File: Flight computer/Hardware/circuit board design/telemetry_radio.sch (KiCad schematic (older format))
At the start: 31 parts, among them U2 AS179-92LF, U3 Si4463, X1 TM-32.000-AF3-33-S-Oscillator

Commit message: added in the RF front end, exactly as stated in AN904
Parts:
- removed ANT2: ICSSPicoTracker_Yageo434, pico_tracker:Yageo434, symbol flight-computer:ICSSPicoTracker_Yageo434
- removed C11, C12, C13: 150pF, Capacitor_SMD:C_0402_1005Metric, symbol Device:C_Small
- removed C14: 12pF, Capacitor_SMD:C_0402_1005Metric, symbol Device:C_Small
- removed C15: 33pF, Capacitor_SMD:C_0402_1005Metric, symbol Device:C_Small
- removed C16: 15pF, Capacitor_SMD:C_0402_1005Metric, symbol Device:C_Small
- removed C17, C27: 4.7pF, Capacitor_SMD:C_0402_1005Metric, symbol Device:C_Small
- removed C18: 9.1pF, Capacitor_SMD:C_0402_1005Metric, symbol Device:C_Small
- removed C24, C25: 1nF, Capacitor_SMD:C_0402_1005Metric, symbol Device:C_Small
- removed C26, C8: NF, Capacitor_SMD:C_0402_1005Metric, symbol Device:C_Small
- removed L2: 0R, Inductor_SMD:L_0402_1005Metric, symbol Device:L
- removed L3: 18nH, Inductor_SMD:L_0402_1005Metric, symbol Device:L
- removed L4: 30nH, Inductor_SMD:L_0402_1005Metric, symbol Device:L
- removed L5: 22nH, Inductor_SMD:L_0402_1005Metric, symbol Device:L
- removed L6, L7: 62nH, Inductor_SMD:L_0402_1005Metric, symbol Device:L
- removed U2: AS179-92LF, Package_TO_SOT_SMD:SOT-363_SC-70-6, symbol RF_Switch:AS179-92LF
- added AE1: Antenna, symbol Device:Antenna
- added C9: 270pF, Capacitor_SMD:C_0402_1005Metric, symbol Device:C_Small
- added J7: Conn_Coaxial, symbol Connector:Conn_Coaxial
- added R4: 0R, symbol Device:R
- added R7: NF, symbol Device:R
- C10: value 2.2uF -> CA
- C19: value 100nf -> 270pf
- gave numbers to parts that had none: 1
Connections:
- net labels removed: RF_GPIO0, RF_GPIO1
- wire segments 112 -> 63
- no-connect marks 4 -> 3
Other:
- note removed: "434 Mhz Antenna Match/Filter"
- note removed: "RF switch"
- note removed: "Rx Balun"
- note removed: "TX Match"
- note removed: "Tx Low Pass Filter"
- moved on the sheet: U2

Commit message: fixed erc problems with Johanson integrated Frontend.
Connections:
- net labels added: RF_GPIO0, RF_GPIO1
- wire segments 63 -> 65
- no-connect marks 3 -> 5
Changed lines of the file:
@@
 Wire Wire Line
 	10050 3650 10050 3900
+Text HLabel 4450 4950 2    50   Input ~ 0
+RF_GPIO0
+Wire Wire Line
+	4450 4950 4200 4950
+Text HLabel 4450 5050 2    50   Input ~ 0
+RF_GPIO1
+Wire Wire Line
+	4450 5050 4200 5050
+NoConn ~ 4200 5250
+NoConn ~ 4200 5150
 $EndSCHEMATC

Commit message: added in some comments
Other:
- note added: "Antenna is wire at 1/4 wavelength. ~17cm"
- note added: "Arranged according to Silabs AN904"
- note added: "Not sure if I should put in the Pi circuit"
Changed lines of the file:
@@
 Sheet 4 7
 Title "Silabs radio chip for telemetry to ground"
-Date "2019-08-31"
-Rev ""
+Date "2019-09-09"
+Rev "1.0"
 Comp "Imperial College Space Society"
-Comment1 "AN629 Figure 16 ideal according to Richard: CLE Switch TX/RX type matching network"
-Comment2 "AN648 for matching network values"
+Comment1 "Arranged according to Silabs AN904."
+Comment2 ""
 Comment3 ""
 Comment4 ""
@@
 NoConn ~ 4200 5250
 NoConn ~ 4200 5150
+Text Notes 8750 2500 0    50   ~ 0
+Not sure if I should put in the Pi circuit
+Text Notes 8800 2700 0    50   ~ 0
+Antenna is wire at 1/4 wavelength. ~17cm
+Text Notes 4550 6100 0    50   ~ 0
+Arranged according to Silabs AN904
 $EndSCHEMATC

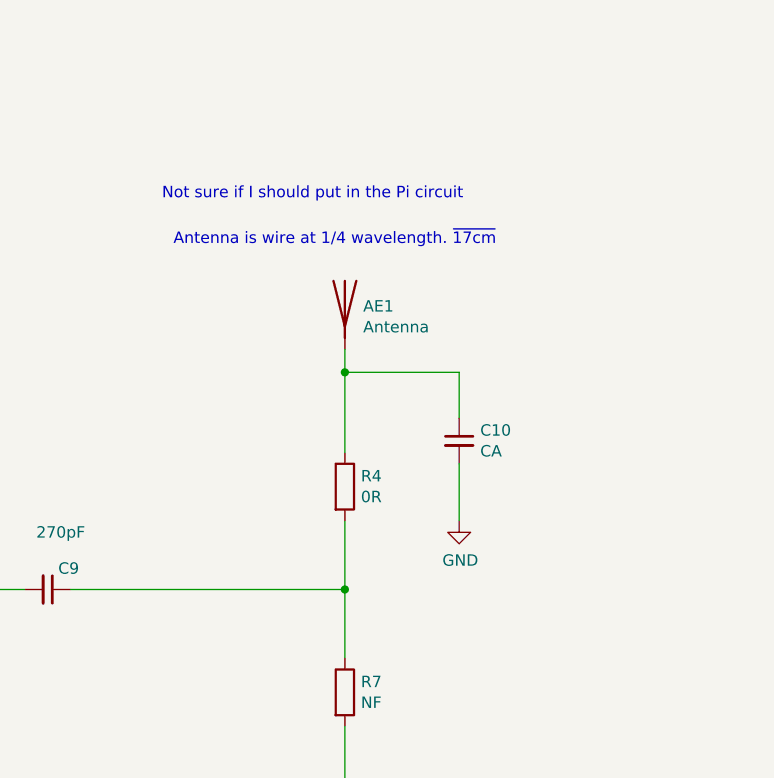
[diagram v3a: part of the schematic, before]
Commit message: completed the pi circuit for Telemetry antenna
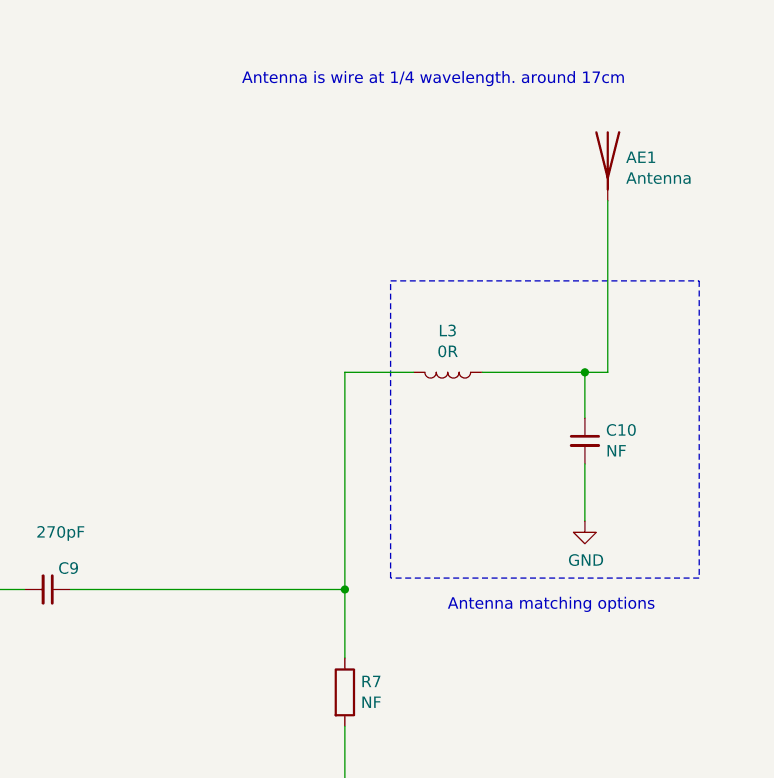
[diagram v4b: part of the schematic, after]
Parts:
- removed R4: 0R, symbol Device:R
- added L3: 0R, Inductor_SMD:L_0402_1005Metric, symbol Device:L
- C10: value CA -> NF
- R7: footprint (none) -> Resistor_SMD:R_0402_1005Metric
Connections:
- wire segments 65 -> 66
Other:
- note added: "Antenna is wire at 1/4 wavelength. around 17cm"
- note added: "Antenna matching options\n"
- note removed: "Antenna is wire at 1/4 wavelength. ~17cm"
- note removed: "Not sure if I should put in the Pi circuit"
- moved on the sheet: AE1
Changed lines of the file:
@@
 L Device:Antenna AE1
 U 1 1 5D79EB91
-P 9550 2950
-F 0 "AE1" H 9630 2939 50  0000 L CNN
-F 1 "Antenna" H 9630 2848 50  0000 L CNN
-F 2 "" H 9550 2950 50  0001 C CNN
-F 3 "~" H 9550 2950 50  0001 C CNN
-	1    9550 2950
+P 10700 2300
+F 0 "AE1" H 10780 2289 50  0000 L CNN
+F 1 "Antenna" H 10780 2198 50  0000 L CNN
+F 2 "" H 10700 2300 50  0001 C CNN
+F 3 "~" H 10700 2300 50  0001 C CNN
+	1    10700 2300
 	1    0    0    -1
 $EndComp
 Wire Wire Line
-	9550 3150 9550 3250
-Wire Wire Line
-	9550 3250 10050 3250
-Wire Wire Line
-	10050 3250 10050 3450
-Connection ~ 9550 3250
-Wire Wire Line
-	9550 3250 9550 3600
-$Comp
-L power:GND #PWR017
-U 1 1 5D7A234E
-P 10050 3900
-F 0 "#PWR017" H 10050 3650 50  0001 C CNN
-F 1 "GND" H 10055 3727 50  0000 C CNN
-F 2 "" H 10050 3900 50  0001 C CNN
-F 3 "" H 10050 3900 50  0001 C CNN
-	1    10050 3900
-	1    0    0    -1
-$EndComp
+	10700 2500 10700 3250
 $Comp
 L Connector:Conn_Coaxial J7
@@
 	3700 2550 3700 2800
 $Comp
-L Device:R R4
-U 1 1 5D7AAB64
-P 9550 3750
-F 0 "R4" H 9620 3796 50  0000 L CNN
-F 1 "0R" H 9620 3705 50  0000 L CNN
-F 2 "" V 9480 3750 50  0001 C CNN
-F 3 "~" H 9550 3750 50  0001 C CNN
-	1    9550 3750
-	1    0    0    -1
-$EndComp
-Wire Wire Line
-	9550 3900 9550 4200
-$Comp
 L Device:R R7
 U 1 1 5D7AB0E5
@@
 F 0 "R7" H 9620 4696 50  0000 L CNN
 F 1 "NF" H 9620 4605 50  0000 L CNN
-F 2 "" V 9480 4650 50  0001 C CNN
+F 2 "Resistor_SMD:R_0402_1005Metric" V 9480 4650 50  0001 C CNN
 F 3 "~" H 9550 4650 50  0001 C CNN
 	1    9550 4650
@@
 Wire Wire Line
 	9550 4800 9550 5050
-$Comp
-L Device:C_Small C10
-U 1 1 5D7AB505
-P 10050 3550
-F 0 "C10" H 9958 3596 50  0000 R CNN
-F 1 "CA" H 9958 3505 50  0000 R CNN
-F 2 "Capacitor_SMD:C_0603_1608Metric" H 10050 3550 50  0001 C CNN
-F 3 "~" H 10050 3550 50  0001 C CNN
-	1    10050 3550
-	-1   0    0    -1
-$EndComp
-Wire Wire Line
-	10050 3650 10050 3900
 Text HLabel 4450 4950 2    50   Input ~ 0
 RF_GPIO0
@@
 NoConn ~ 4200 5250
 NoConn ~ 4200 5150
-Text Notes 8750 2500 0    50   ~ 0
-Not sure if I should put in the Pi circuit
-Text Notes 8800 2700 0    50   ~ 0
-Antenna is wire at 1/4 wavelength. ~17cm
+Text Notes 9100 2000 0    50   ~ 0
+Antenna is wire at 1/4 wavelength. around 17cm
 Text Notes 4550 6100 0    50   ~ 0
 Arranged according to Silabs AN904
+Wire Wire Line
+	10150 3250 10600 3250
+Wire Wire Line
+	9550 3250 9550 4200
+Wire Wire Line
+	10600 3650 10600 3900
+$Comp
+L Device:C_Small C10
+U 1 1 5D7EC7D6
+P 10600 3550
+F 0 "C10" H 10508 3596 50  0000 R CNN
+F 1 "NF" H 10508 3505 50  0000 R CNN
+F 2 "Capacitor_SMD:C_0603_1608Metric" H 10600 3550 50  0001 C CNN
+F 3 "~" H 10600 3550 50  0001 C CNN
+	1    10600 3550
+	-1   0    0    -1
+$EndComp
+$Comp
+L power:GND #PWR07
+U 1 1 5D7EC7E0
+P 10600 3900
+F 0 "#PWR07" H 10600 3650 50  0001 C CNN
+F 1 "GND" H 10605 3727 50  0000 C CNN
+F 2 "" H 10600 3900 50  0001 C CNN
+F 3 "" H 10600 3900 50  0001 C CNN
+	1    10600 3900
+	1    0    0    -1
+$EndComp
+Wire Wire Line
+	10600 3250 10600 3450
+Connection ~ 10600 3250
+Wire Wire Line
+	10600 3250 10700 3250
+Text Notes 10000 4300 0    50   ~ 0
+Antenna matching options\n
+Wire Wire Line
+	9550 3250 9850 3250
+$Comp
+L Device:L L3
+U 1 1 5D7F0545
+P 10000 3250
+F 0 "L3" V 9819 3250 50  0000 C CNN
+F 1 "0R" V 9910 3250 50  0000 C CNN
+F 2 "Inductor_SMD:L_0402_1005Metric" H 10000 3250 50  0001 C CNN
+F 3 "~" H 10000 3250 50  0001 C CNN
+	1    10000 3250
+	0    1    1    0
+$EndComp
+Wire Notes Line
+	11100 4150 9750 4150
+Wire Notes Line
+	9750 4150 9750 2850
+Wire Notes Line
+	9750 2850 11100 2850
+Wire Notes Line
+	11100 2850 11100 4150
 $EndSCHEMATC

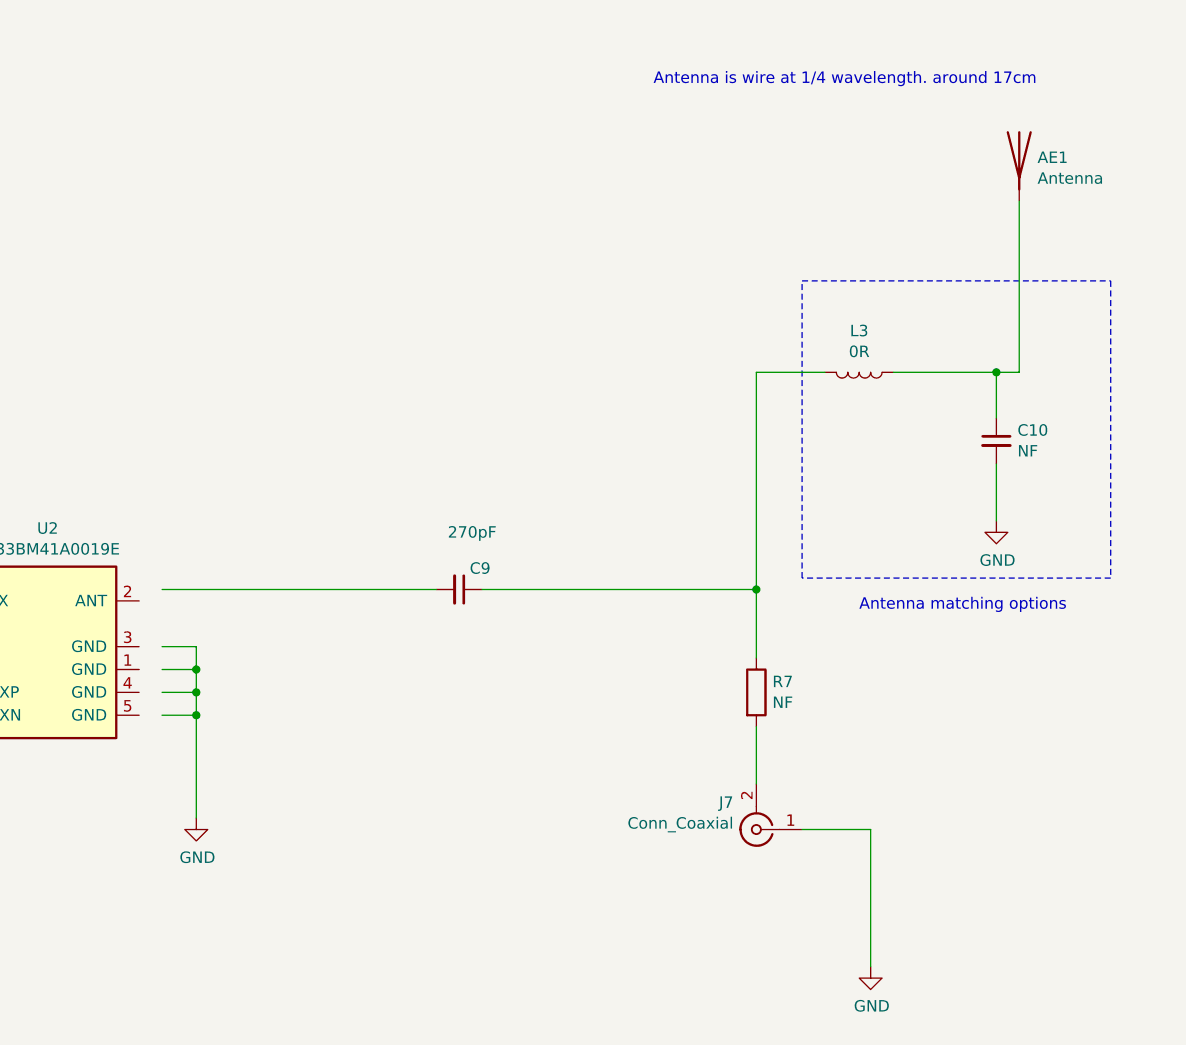
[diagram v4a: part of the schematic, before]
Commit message: changed the pin header to 2.54mm pitch for programmer and added a 3 pin header for antenna 434
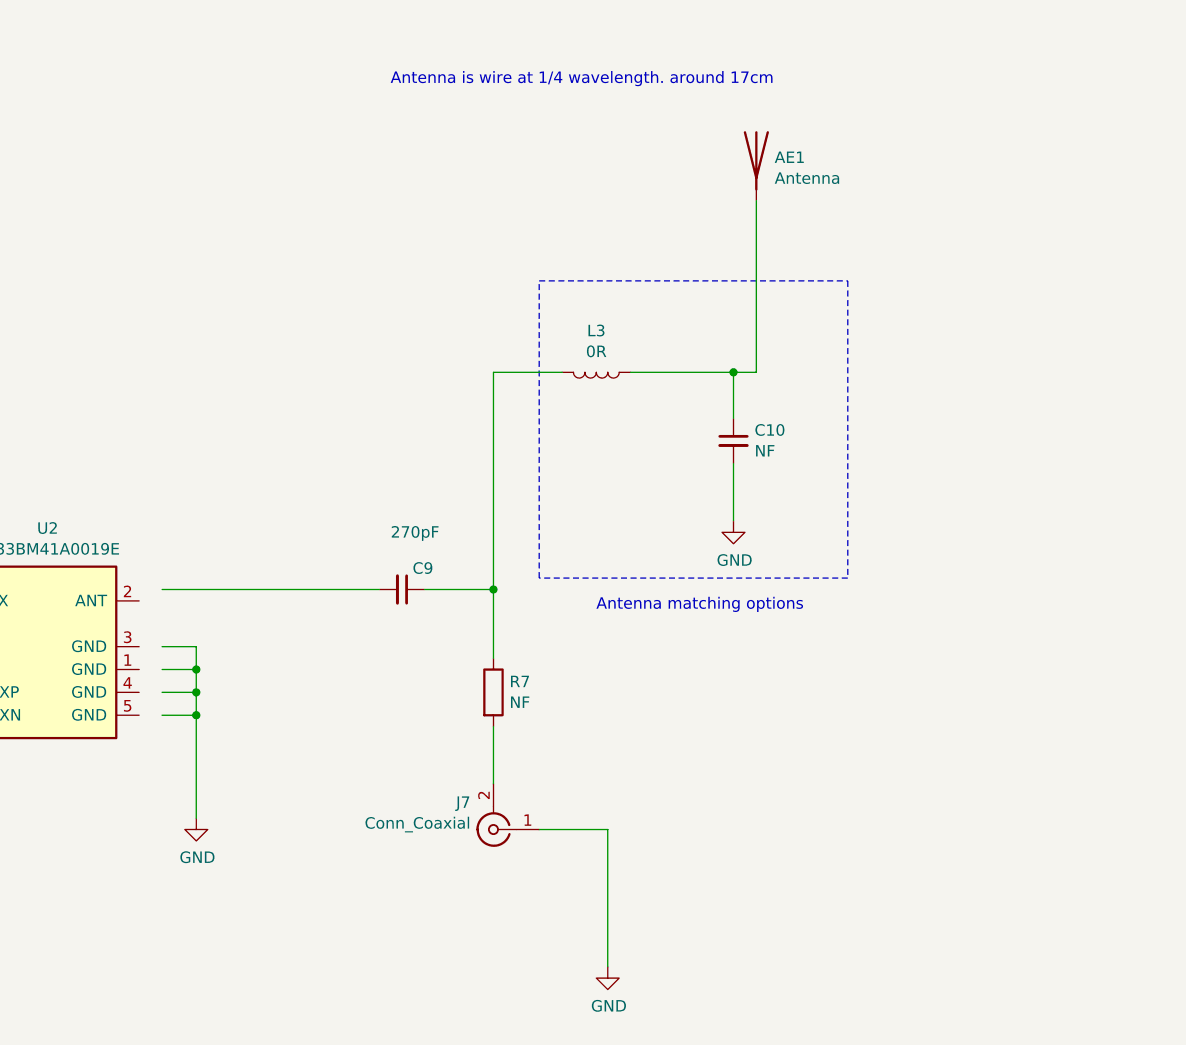
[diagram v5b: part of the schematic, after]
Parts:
- AE1: footprint (none) -> Connector_PinHeader_1.00mm:PinHeader_1x03_P1.00mm_Vertical
- J7: footprint (none) -> Connector_Coaxial:U.FL_Hirose_U.FL-R-SMT-1_Vertical
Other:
- moved on the sheet: AE1, C10, C9, J7, L3, R7
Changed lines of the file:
@@
 $EndComp
 Wire Wire Line
-	6950 4200 8150 4200
+	6950 4200 7900 4200
 $Comp
 L Device:C_Small C9
 U 1 1 5D796ABE
-P 8250 4200
-F 0 "C9" V 8342 4246 50  0000 L CNN
-F 1 "270pF" V 8500 4150 50  0000 L CNN
-F 2 "Capacitor_SMD:C_0402_1005Metric" H 8250 4200 50  0001 C CNN
-F 3 "~" H 8250 4200 50  0001 C CNN
-	1    8250 4200
+P 8000 4200
+F 0 "C9" V 8092 4246 50  0000 L CNN
+F 1 "270pF" V 8250 4150 50  0000 L CNN
+F 2 "Capacitor_SMD:C_0402_1005Metric" H 8000 4200 50  0001 C CNN
+F 3 "~" H 8000 4200 50  0001 C CNN
+	1    8000 4200
 	0    1    -1   0
-$EndComp
-Wire Wire Line
-	8350 4200 9550 4200
-Wire Wire Line
-	9550 4200 9550 4500
-Connection ~ 9550 4200
-$Comp
-L Device:Antenna AE1
-U 1 1 5D79EB91
-P 10700 2300
-F 0 "AE1" H 10780 2289 50  0000 L CNN
-F 1 "Antenna" H 10780 2198 50  0000 L CNN
-F 2 "" H 10700 2300 50  0001 C CNN
-F 3 "~" H 10700 2300 50  0001 C CNN
-	1    10700 2300
-	1    0    0    -1
-$EndComp
-Wire Wire Line
-	10700 2500 10700 3250
-$Comp
-L Connector:Conn_Coaxial J7
-U 1 1 5D7A2CE8
-P 9550 5250
-F 0 "J7" H 9650 5132 50  0000 L CNN
-F 1 "Conn_Coaxial" H 9650 5223 50  0000 L CNN
-F 2 "" H 9550 5250 50  0001 C CNN
-F 3 " ~" H 9550 5250 50  0001 C CNN
-	1    9550 5250
-	-1   0    0    1
-$EndComp
-Wire Wire Line
-	9750 5250 10050 5250
-Wire Wire Line
-	10050 5250 10050 5850
-$Comp
-L power:GND #PWR028
-U 1 1 5D7A6387
-P 10050 5850
-F 0 "#PWR028" H 10050 5600 50  0001 C CNN
-F 1 "GND" H 10055 5677 50  0000 C CNN
-F 2 "" H 10050 5850 50  0001 C CNN
-F 3 "" H 10050 5850 50  0001 C CNN
-	1    10050 5850
-	1    0    0    -1
 $EndComp
 Wire Wire Line
@@
 Wire Wire Line
 	3700 2550 3700 2800
-$Comp
-L Device:R R7
-U 1 1 5D7AB0E5
-P 9550 4650
-F 0 "R7" H 9620 4696 50  0000 L CNN
-F 1 "NF" H 9620 4605 50  0000 L CNN
-F 2 "Resistor_SMD:R_0402_1005Metric" V 9480 4650 50  0001 C CNN
-F 3 "~" H 9550 4650 50  0001 C CNN
-	1    9550 4650
-	1    0    0    -1
-$EndComp
-Wire Wire Line
-	9550 4800 9550 5050
 Text HLabel 4450 4950 2    50   Input ~ 0
 RF_GPIO0
@@
 NoConn ~ 4200 5250
 NoConn ~ 4200 5150
-Text Notes 9100 2000 0    50   ~ 0
+Text Notes 7950 2000 0    50   ~ 0
 Antenna is wire at 1/4 wavelength. around 17cm
 Text Notes 4550 6100 0    50   ~ 0
 Arranged according to Silabs AN904
+Wire Notes Line
+	9950 2850 9950 4150
+Wire Notes Line
+	8600 2850 9950 2850
+Wire Notes Line
+	8600 4150 8600 2850
+Wire Notes Line
+	9950 4150 8600 4150
+$Comp
+L Device:L L3
+U 1 1 5D7F0545
+P 8850 3250
+F 0 "L3" V 8669 3250 50  0000 C CNN
+F 1 "0R" V 8760 3250 50  0000 C CNN
+F 2 "Inductor_SMD:L_0402_1005Metric" H 8850 3250 50  0001 C CNN
+F 3 "~" H 8850 3250 50  0001 C CNN
+	1    8850 3250
+	0    1    1    0
+$EndComp
 Wire Wire Line
-	10150 3250 10600 3250
+	8400 3250 8700 3250
+Text Notes 8850 4300 0    50   ~ 0
+Antenna matching options\n
 Wire Wire Line
-	9550 3250 9550 4200
+	9450 3250 9550 3250
+Connection ~ 9450 3250
 Wire Wire Line
-	10600 3650 10600 3900
+	9450 3250 9450 3450
+$Comp
+L power:GND #PWR07
+U 1 1 5D7EC7E0
+P 9450 3900
+F 0 "#PWR07" H 9450 3650 50  0001 C CNN
+F 1 "GND" H 9455 3727 50  0000 C CNN
+F 2 "" H 9450 3900 50  0001 C CNN
+F 3 "" H 9450 3900 50  0001 C CNN
+	1    9450 3900
+	1    0    0    -1
+$EndComp
 $Comp
 L Device:C_Small C10
 U 1 1 5D7EC7D6
-P 10600 3550
-F 0 "C10" H 10508 3596 50  0000 R CNN
-F 1 "NF" H 10508 3505 50  0000 R CNN
-F 2 "Capacitor_SMD:C_0603_1608Metric" H 10600 3550 50  0001 C CNN
-F 3 "~" H 10600 3550 50  0001 C CNN
-	1    10600 3550
+P 9450 3550
+F 0 "C10" H 9358 3596 50  0000 R CNN
+F 1 "NF" H 9358 3505 50  0000 R CNN
+F 2 "Capacitor_SMD:C_0603_1608Metric" H 9450 3550 50  0001 C CNN
+F 3 "~" H 9450 3550 50  0001 C CNN
+	1    9450 3550
 	-1   0    0    -1
 $EndComp
+Wire Wire Line
+	9450 3650 9450 3900
+Wire Wire Line
+	8400 3250 8400 4200
+Wire Wire Line
+	9000 3250 9450 3250
+Wire Wire Line
+	8400 4800 8400 5050
 $Comp
-L power:GND #PWR07
-U 1 1 5D7EC7E0
-P 10600 3900
-F 0 "#PWR07" H 10600 3650 50  0001 C CNN
-F 1 "GND" H 10605 3727 50  0000 C CNN
-F 2 "" H 10600 3900 50  0001 C CNN
-F 3 "" H 10600 3900 50  0001 C CNN
-	1    10600 3900
+L Device:R R7
+U 1 1 5D7AB0E5
+P 8400 4650
+F 0 "R7" H 8470 4696 50  0000 L CNN
+F 1 "NF" H 8470 4605 50  0000 L CNN
+F 2 "Resistor_SMD:R_0402_1005Metric" V 8330 4650 50  0001 C CNN
+F 3 "~" H 8400 4650 50  0001 C CNN
+	1    8400 4650
+	1    0    0    -1
+$EndComp
+$Comp
+L power:GND #PWR028
+U 1 1 5D7A6387
+P 8900 5850
+F 0 "#PWR028" H 8900 5600 50  0001 C CNN
+F 1 "GND" H 8905 5677 50  0000 C CNN
+F 2 "" H 8900 5850 50  0001 C CNN
+F 3 "" H 8900 5850 50  0001 C CNN
+	1    8900 5850
 	1    0    0    -1
 $EndComp
 Wire Wire Line
-	10600 3250 10600 3450
-Connection ~ 10600 3250
+	8900 5250 8900 5850
 Wire Wire Line
-	10600 3250 10700 3250
-Text Notes 10000 4300 0    50   ~ 0
-Antenna matching options\n
+	8600 5250 8900 5250
+$Comp
+L Connector:Conn_Coaxial J7
+U 1 1 5D7A2CE8
+P 8400 5250
+F 0 "J7" H 8500 5132 50  0000 L CNN
+F 1 "Conn_Coaxial" H 8500 5223 50  0000 L CNN
+F 2 "Connector_Coaxial:U.FL_Hirose_U.FL-R-SMT-1_Vertical" H 8400 5250 50  0001 C CNN
+F 3 " ~" H 8400 5250 50  0001 C CNN
+	1    8400 5250
+	-1   0    0    1
+$EndComp
+Connection ~ 8400 4200
 Wire Wire Line
-	9550 3250 9850 3250
+	8400 4200 8400 4500
+Wire Wire Line
+	8100 4200 8400 4200
+Wire Wire Line
+	9550 2500 9550 3250
 $Comp
-L Device:L L3
-U 1 1 5D7F0545
-P 10000 3250
-F 0 "L3" V 9819 3250 50  0000 C CNN
-F 1 "0R" V 9910 3250 50  0000 C CNN
-F 2 "Inductor_SMD:L_0402_1005Metric" H 10000 3250 50  0001 C CNN
-F 3 "~" H 10000 3250 50  0001 C CNN
-	1    10000 3250
-	0    1    1    0
+L Device:Antenna AE1
+U 1 1 5D79EB91
+P 9550 2300
+F 0 "AE1" H 9630 2289 50  0000 L CNN
+F 1 "Antenna" H 9630 2198 50  0000 L CNN
+F 2 "Connector_PinHeader_1.00mm:PinHeader_1x03_P1.00mm_Vertical" H 9550 2300 50  0001 C CNN
+F 3 "~" H 9550 2300 50  0001 C CNN
+	1    9550 2300
+	1    0    0    -1
 $EndComp
-Wire Notes Line
-	11100 4150 9750 4150
-Wire Notes Line
-	9750 4150 9750 2850
-Wire Notes Line
-	9750 2850 11100 2850
-Wire Notes Line
-	11100 2850 11100 4150
 $EndSCHEMATC
